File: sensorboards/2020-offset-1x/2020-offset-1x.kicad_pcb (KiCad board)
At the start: 2 copper layers, 8 x 46.2 mm, 7 parts, among them J1 Conn_02x02_Odd_Even, U1 CNY70

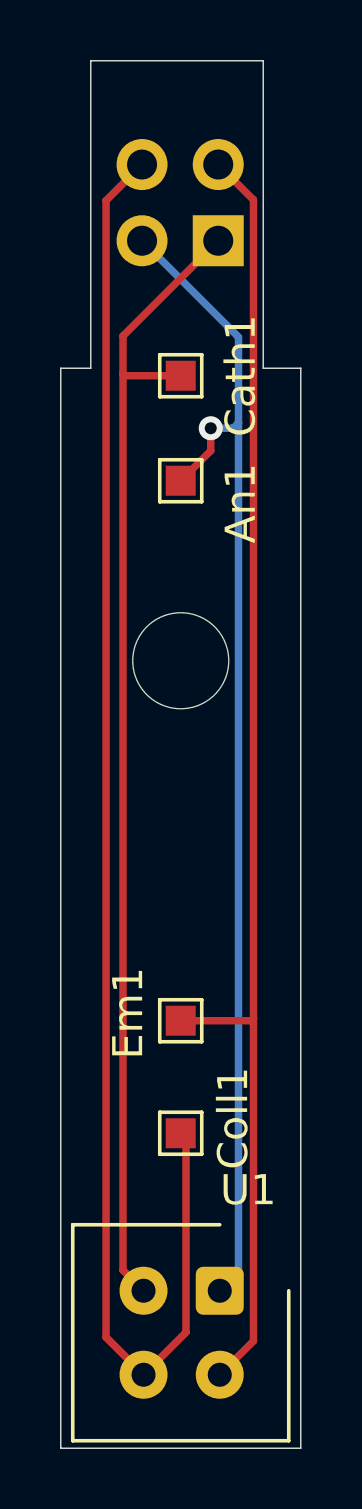
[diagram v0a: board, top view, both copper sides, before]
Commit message: Made issue #44 changes to sensorboards, introduced 3x versions
Also finished bringing them up to Kicad 6.0
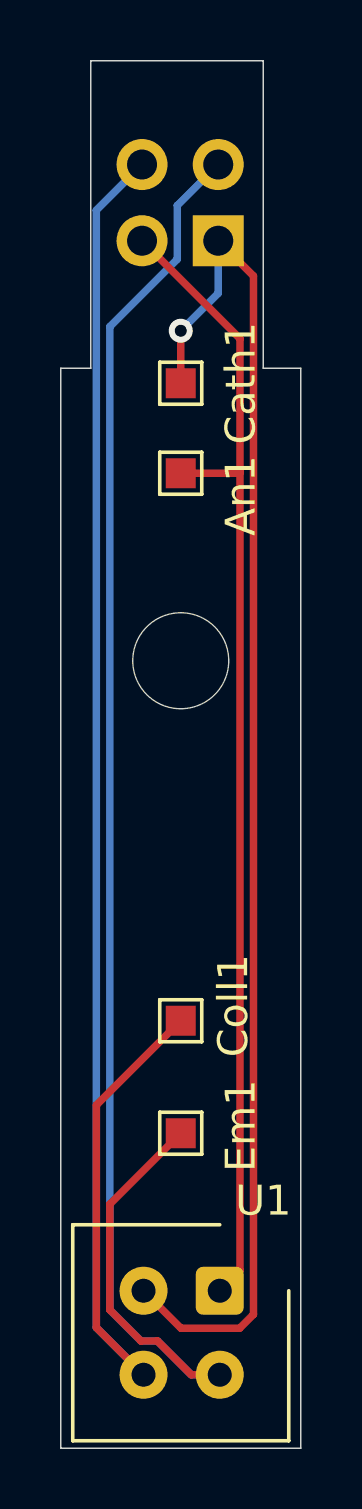
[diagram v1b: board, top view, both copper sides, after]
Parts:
- moved Coll1 3.75 mm to (175.0, 122.0)
- moved Em1 3.75 mm to (175.0, 125.8)
- moved An1 0.25 mm to (175.0, 103.8)
- moved Cath1 0.25 mm to (175.0, 100.8)
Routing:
- net /Emitter: track 43.7 -> 55.7 mm
- net /Cathode: track 38.6 -> 45.9 mm, vias 0 -> 1
- net /Collector: track 50.1 -> 55.2 mm
- net /Anode: track 39.8 -> 39.5 mm, vias 1 -> 0
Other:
- net class Default removed
